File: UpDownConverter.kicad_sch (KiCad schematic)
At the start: 0 parts

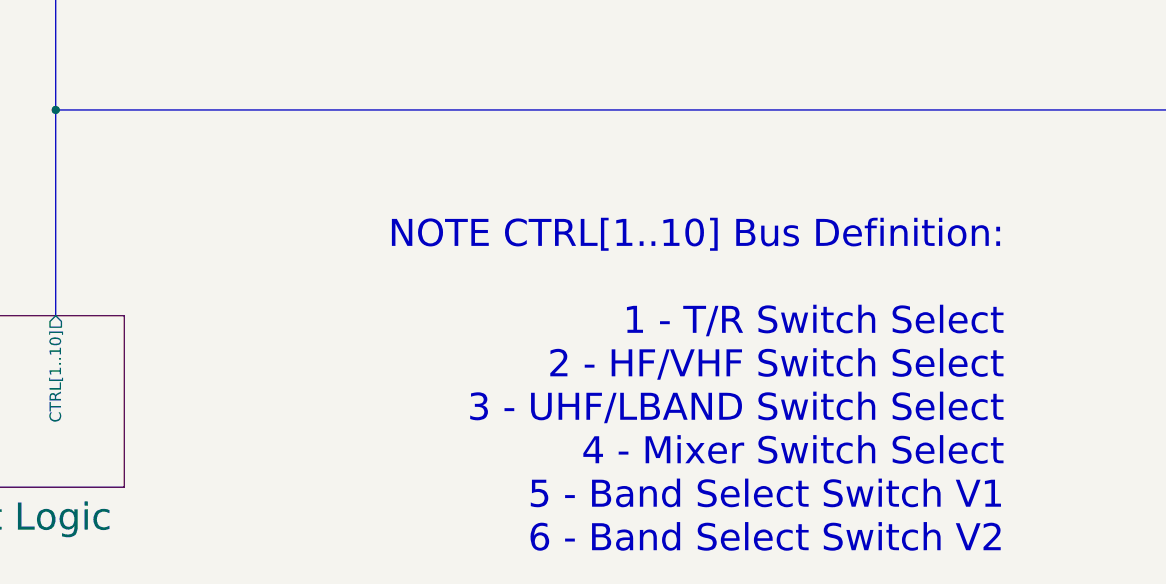
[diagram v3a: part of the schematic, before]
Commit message: Replace DDS with VCOs + a switch.
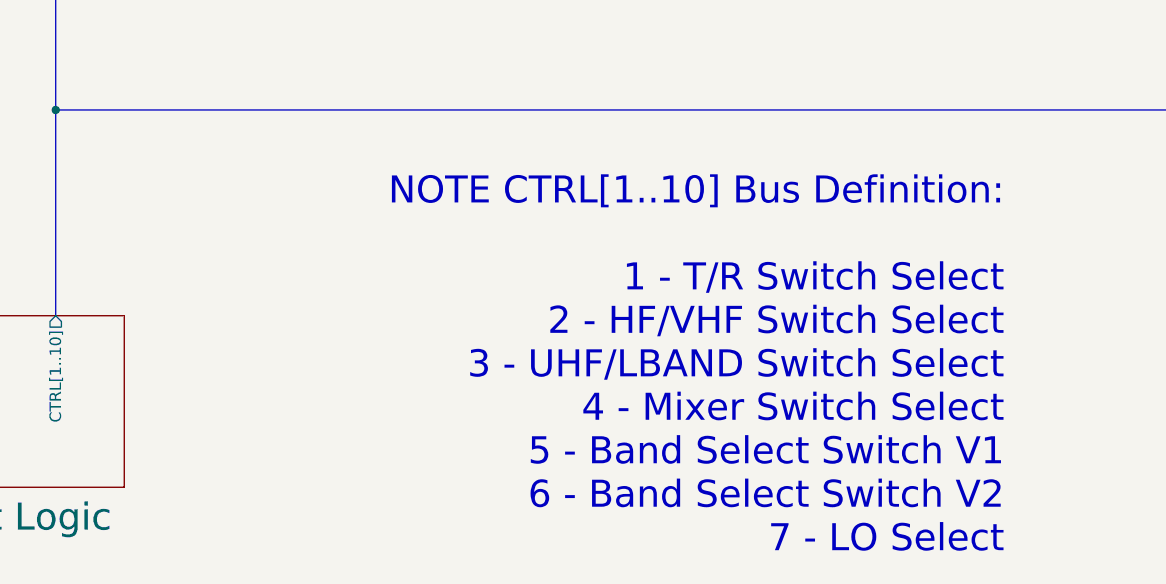
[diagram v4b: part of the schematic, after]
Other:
- note added: "NOTE CTRL[1..10] Bus Definition: 1 - T/R Switch Select 2 - HF/VHF Switch Select 3 - UHF/LBAND Switch Select 4 - Mixer Switch Select 5 - Band Select Switch V1 6 - Band Select Switch V2 7 - LO Select"
- note removed: "NOTE CTRL[1..10] Bus Definition: 1 - T/R Switch Select 2 - HF/VHF Switch Select 3 - UHF/LBAND Switch Select 4 - Mixer Switch Select 5 - Band Select Switch V1 6 - Band Select Switch V2"
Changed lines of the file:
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@@
     (stroke (width 0) (type default))
   )
-  (text "NOTE CTRL[1..10] Bus Definition:\n\n1 - T/R Switch Select\n2 - HF/VHF Switch Select\n3 - UHF/LBAND Switch Select\n4 - Mixer Switch Select\n5 - Band Select Switch V1\n6 - Band Select Switch V2\n"
+  (text "NOTE CTRL[1..10] Bus Definition:\n\n1 - T/R Switch Select\n2 - HF/VHF Switch Select\n3 - UHF/LBAND Switch Select\n4 - Mixer Switch Select\n5 - Band Select Switch V1\n6 - Band Select Switch V2\n7 - LO Select\n"
     (at 227.33 200.66 0)
     (effects (font (size 3 3)) (justify right bottom))
